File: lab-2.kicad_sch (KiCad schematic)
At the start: 30 parts, among them J1 Conn_01x04_Pin, J2 USB_C_Receptacle, SW1 NRST, SW2 BOOT, U1 LM66100DCK, U2 LM66100DCK, U3 STM32F405RGTx, U4 MCP1700x-120xxMB, Y1 8 MHz

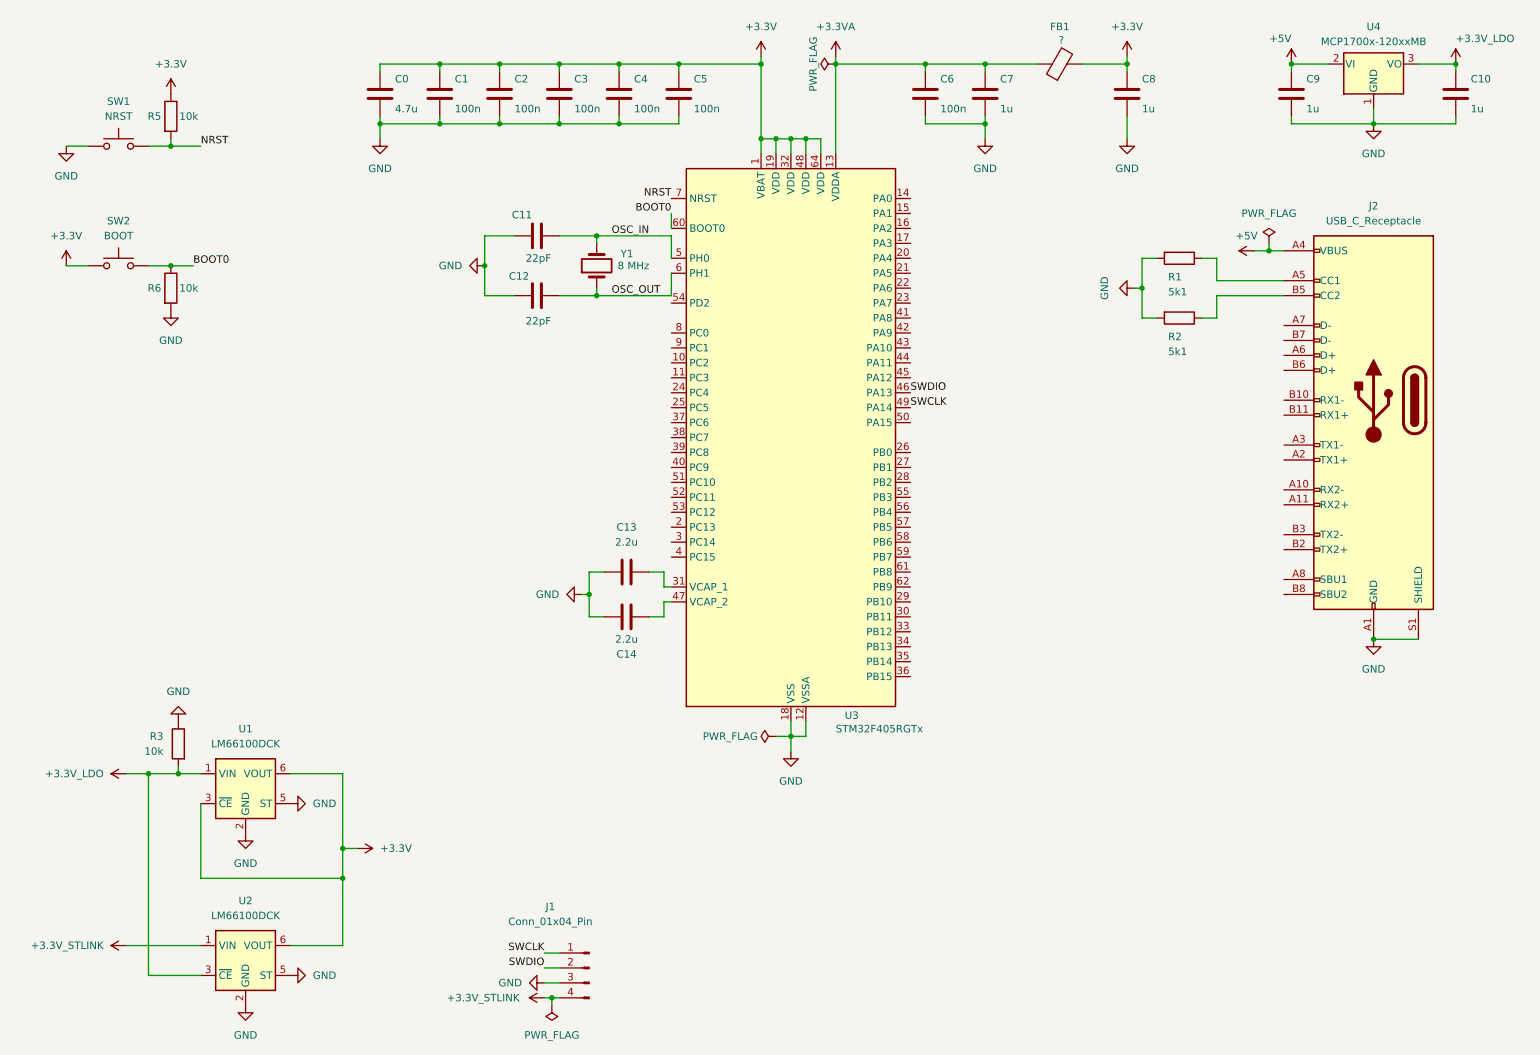
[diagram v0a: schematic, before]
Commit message: Added 2 new layers + GPIO port A (4 pins)
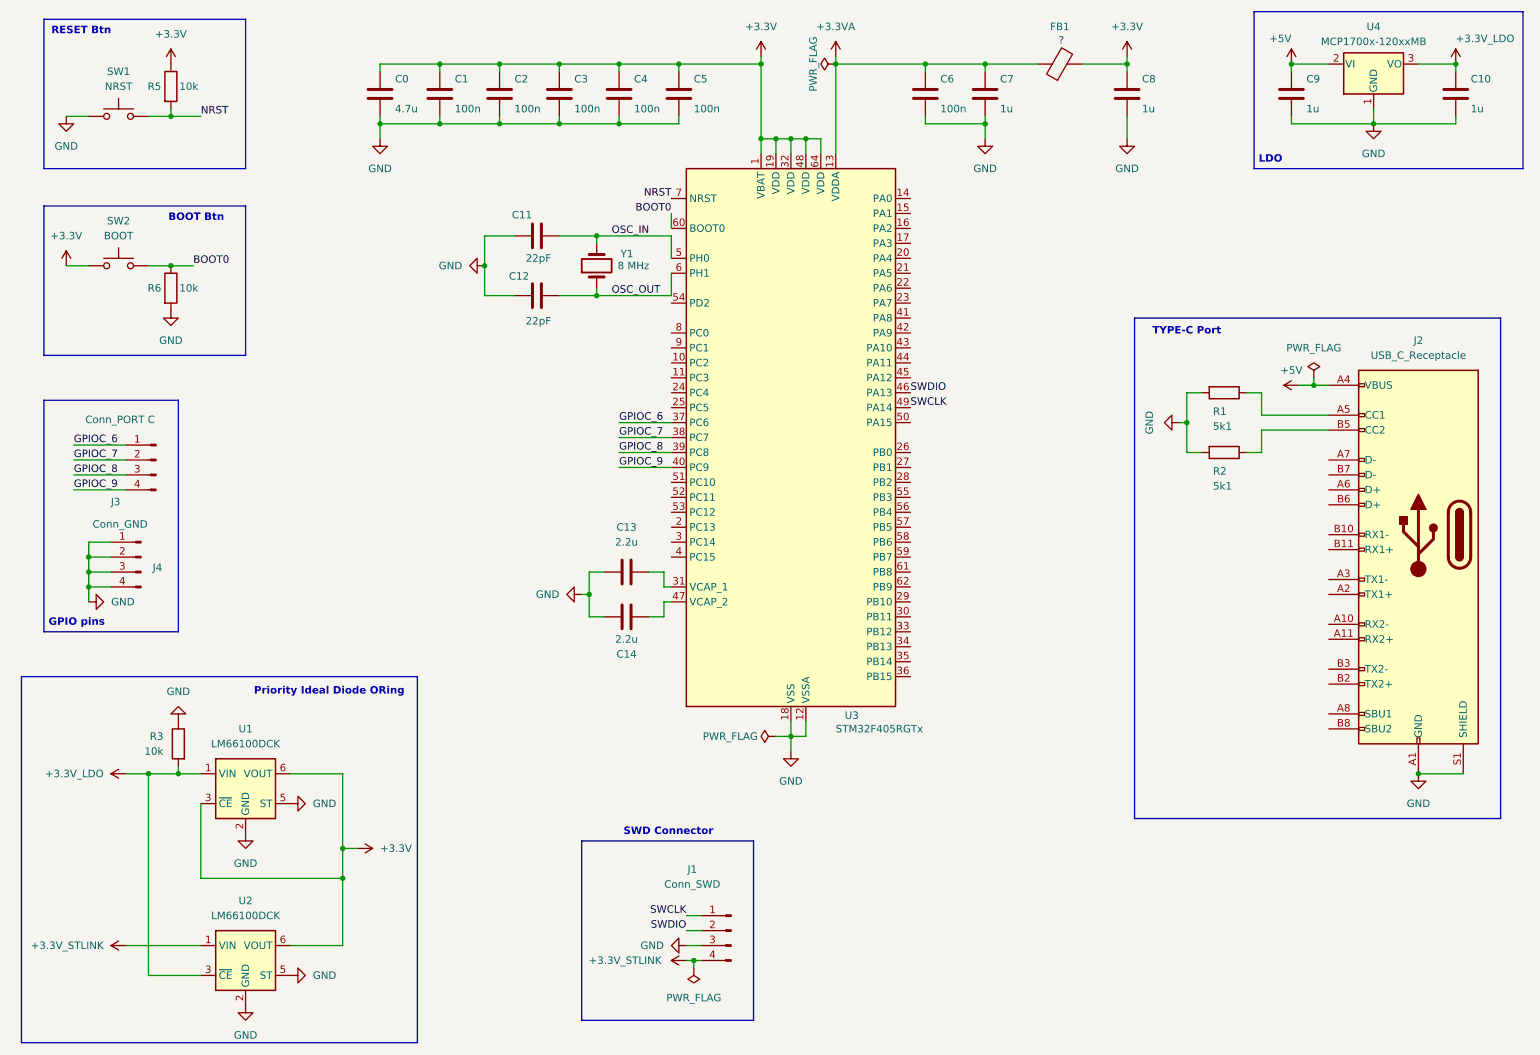
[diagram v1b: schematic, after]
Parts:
- added J3: Conn_PORT C, Connector_PinHeader_2.54mm:PinHeader_1x04_P2.54mm_Vertical, symbol Connector:Conn_01x04_Pin
- added J4: Conn_GND, Connector_PinHeader_2.54mm:PinHeader_1x04_P2.54mm_Vertical, symbol Connector:Conn_01x04_Pin
- J1: value Conn_01x04_Pin -> Conn_SWD
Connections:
- net GND: now also J4.1 (Pin_1), J4.2 (Pin_2), J4.3 (Pin_3), J4.4 (Pin_4)
- net GPIOC_6: now reaches U3.37 (PC6)
- net GPIOC_6: now also J3.1 (Pin_1)
- net GPIOC_7: now reaches U3.38 (PC7)
- net GPIOC_7: now also J3.2 (Pin_2)
- net GPIOC_8: now reaches U3.39 (PC8)
- net GPIOC_8: now also J3.3 (Pin_3)
- net GPIOC_9: now reaches U3.40 (PC9)
- net GPIOC_9: now also J3.4 (Pin_4)
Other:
- note added: "BOOT Btn"
- note added: "GPIO pins"
- note added: "LDO"
- note added: "Priority Ideal Diode ORing"
- note added: "RESET Btn"
- note added: "SWD Connector"
- note added: "TYPE-C Port"
- moved on the sheet: J1, J2, R1, R2, R5, SW1

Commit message: add USER button and LEDs
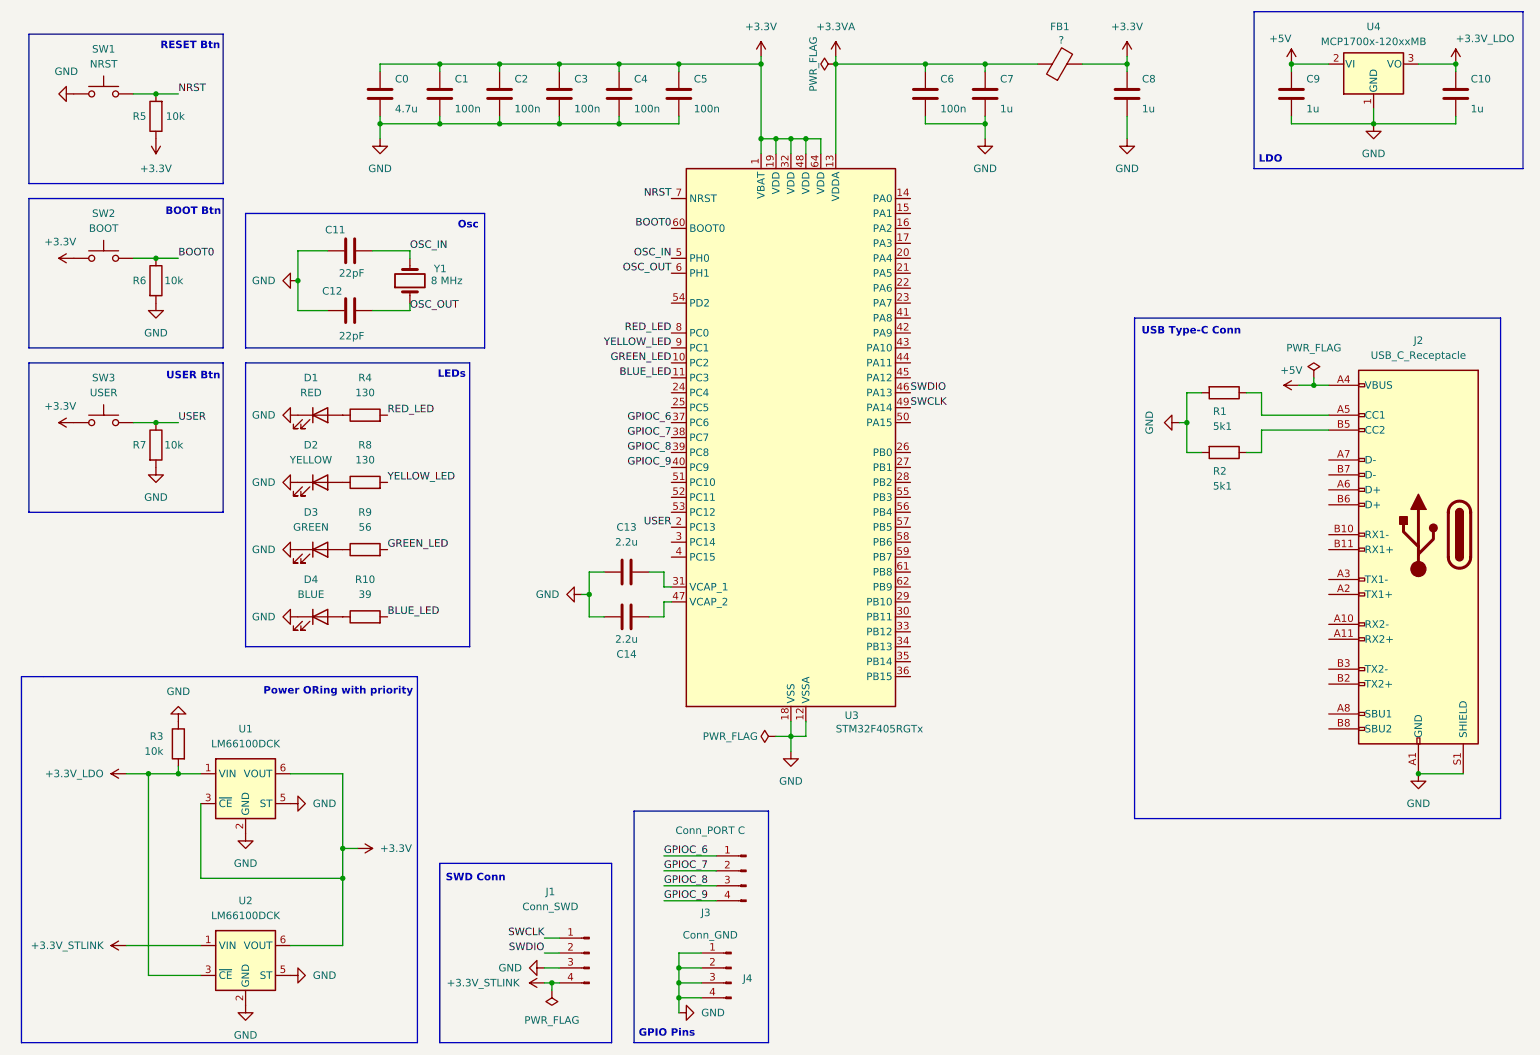
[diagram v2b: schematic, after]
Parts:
- added D1: RED, LED_SMD:LED_0805_2012Metric, symbol Device:LED
- added D2: YELLOW, LED_SMD:LED_0805_2012Metric, symbol Device:LED
- added D3: GREEN, LED_SMD:LED_0805_2012Metric, symbol Device:LED
- added D4: BLUE, LED_SMD:LED_0805_2012Metric, symbol Device:LED
- added R10: 39, Resistor_SMD:R_0402_1005Metric, symbol Device:R
- added R4, R8: 130, Resistor_SMD:R_0402_1005Metric, symbol Device:R
- added R7: 10k, Resistor_SMD:R_0402_1005Metric, symbol Device:R
- added R9: 56, Resistor_SMD:R_0402_1005Metric, symbol Device:R
- added SW3: USER, Button_Switch_SMD:SW_SPST_PTS647_Sx38, symbol Switch:SW_Push
- SW1, SW2: footprint Button_Switch_THT:SW_PUSH_6mm_H4.3mm -> Button_Switch_SMD:SW_SPST_PTS647_Sx38
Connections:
- net +3.3V: now also SW3.2
- net GND: now also D1.1 (K), D2.1 (K), D3.1 (K), D4.1 (K), R7.2
- net GREEN_LED: now reaches U3.10 (PC2)
- net GREEN_LED: now also R9.2
- net BLUE_LED: now reaches U3.11 (PC3)
- net BLUE_LED: now also R10.2
- net USER: now reaches U3.2 (PC13)
- net USER: now also R7.1, SW3.1
- net RED_LED: now reaches U3.8 (PC0)
- net RED_LED: now also R4.2
- net YELLOW_LED: now reaches U3.9 (PC1)
- net YELLOW_LED: now also R8.2
- new net: D1.2 (A), R4.1
- new net: D4.2 (A), R10.1
- new net: D3.2 (A), R9.1
- new net: D2.2 (A), R8.1
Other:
- note added: "GPIO Pins"
- note added: "LEDs"
- note added: "Osc"
- note added: "Power ORing with priority"
- note added: "SWD Conn"
- note added: "USB Type-C Conn"
- note added: "USER Btn"
- note removed: "GPIO pins"
- note removed: "Priority Ideal Diode ORing"
- note removed: "SWD Connector"
- note removed: "TYPE-C Port"
- moved on the sheet: C11, C12, J1, J3, J4, R5, R6, SW1, SW2, Y1

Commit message: added potentiometer
Signed-off-by: Yehor Bilous <bilous801@gmail.com>
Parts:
- added RV1: R_Potentiometer_Small, Potentiometer_SMD:Potentiometer_Bourns_3224G_Horizontal, symbol Device:R_Potentiometer_Small
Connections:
- net +3.3V: now also RV1.1
- net GND: now also RV1.3
- net POT_ADC: now reaches U3.15 (PA1)
- net POT_ADC: now also RV1.2

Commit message: fix some ERC and DRC issues
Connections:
- net GND: now also J2.SH (SHIELD); no longer J2.S1 (SHIELD)
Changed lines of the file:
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@@
+			)
+		)
+		(property "Sim.Device" "R"
+			(at 190.5 151.13 0)
+			(hide yes)
+			(show_name no)
+			(do_not_autoplace no)
+			(effects
+				(font
+					(size 1.27 1.27)
+				)
+			)
+		)
+		(property "Sim.Type" "POT"
+			(at 190.5 151.13 0)
+			(hide yes)
+			(show_name no)
+			(do_not_autoplace no)
+			(effects
+				(font
+					(size 1.27 1.27)
+				)
+			)
+		)
+		(property "Sim.Pins" "1=r0 2=wiper 3=r1"
+			(at 190.5 151.13 0)
+			(hide yes)
+			(show_name no)
+			(do_not_autoplace no)
+			(effects
+				(font
+					(size 1.27 1.27)
+				)
 			)
 		)
@@
 		(pin "B10"
 		)
-		(pin "S1"
+		(pin "SH"
 		)
 		(pin "B3"
